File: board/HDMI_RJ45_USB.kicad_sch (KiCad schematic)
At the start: 10 parts, among them J1 RJ45, J2 Micro_SD_Card_Det, U1 HDMI/USB, U11 TPD4EUSB30, U12 RT9742GGJ5, U5 RT9742GGJ5, U6 TPD4EUSB30

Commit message: updated most stuff, but i completely redid the diff pairs
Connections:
- net TRD1_N: now also U6.1 (D1+); no longer U6.2 (D1-)
- net TRD1_P: now also U6.2 (D1-); no longer U6.1 (D1+)
- net TRD2_N: now also U11.5 (D2-); no longer U11.4 (D2+)
- net TRD2_P: now also U11.4 (D2+); no longer U11.5 (D2-)
- net TRD3_N: now also U11.1 (D1+); no longer U11.2 (D1-)
- net TRD3_P: now also U11.2 (D1-); no longer U11.1 (D1+)

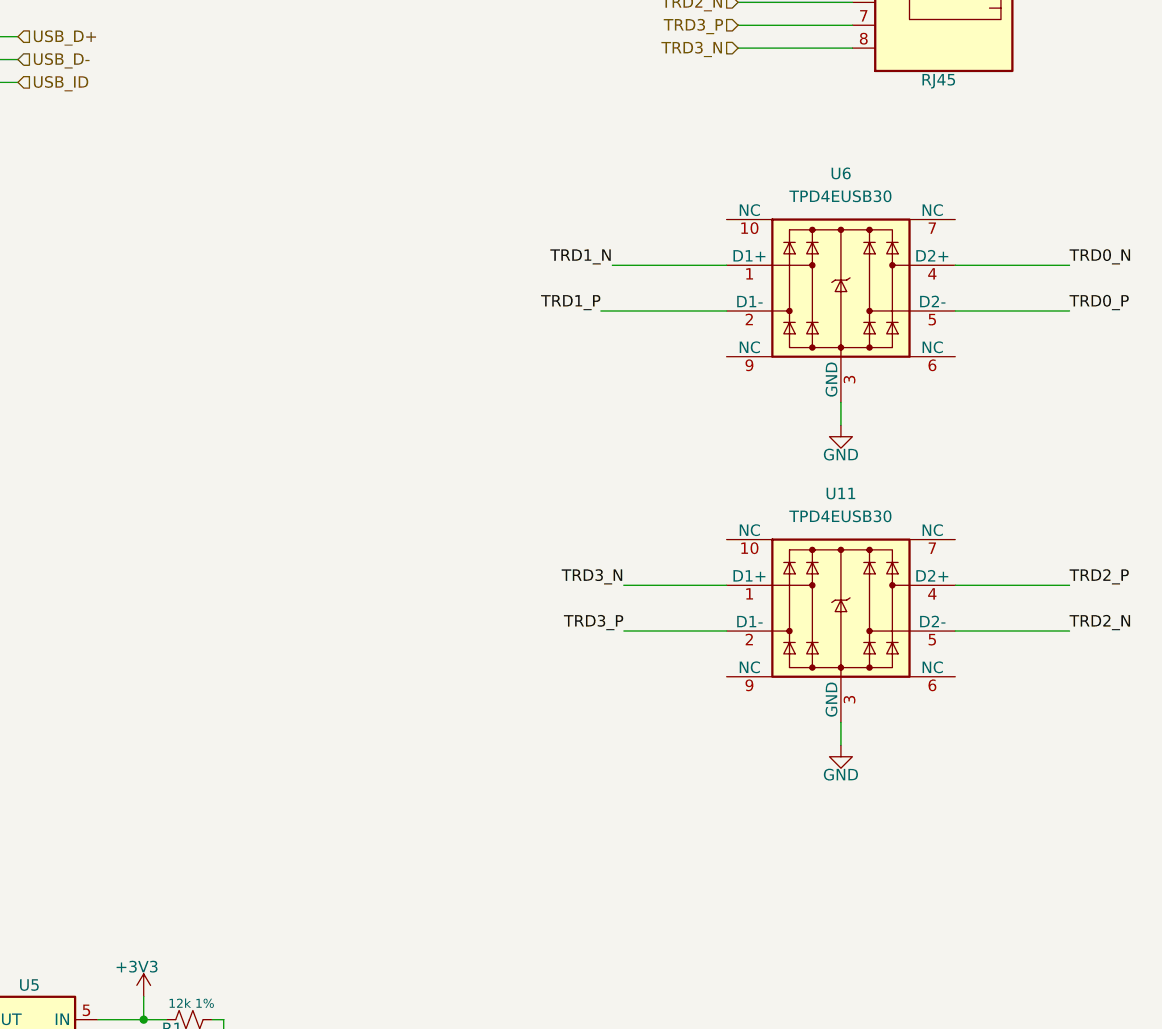
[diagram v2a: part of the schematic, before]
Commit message: going to add the magnetic transformer which will messs a lot of stuff up
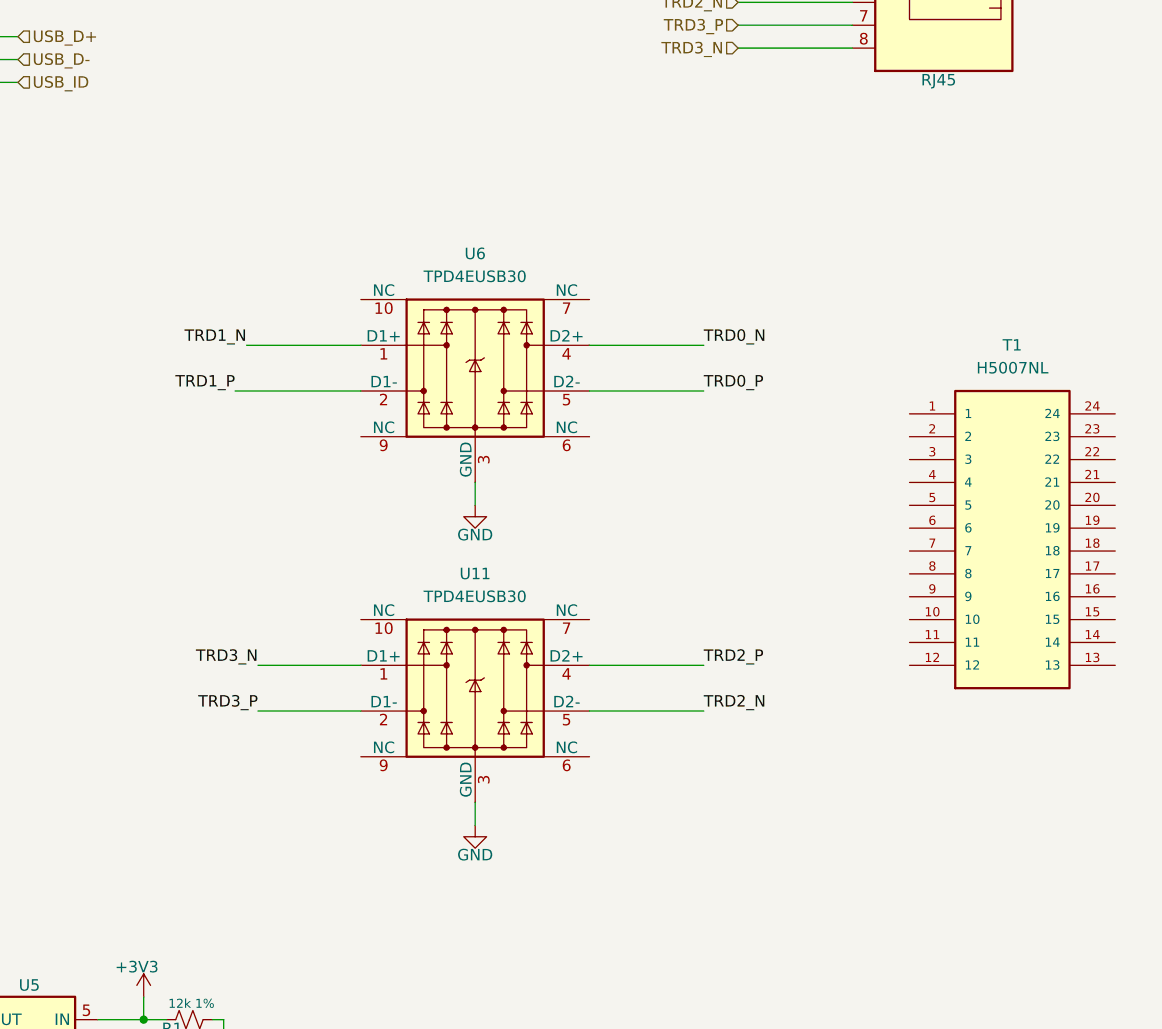
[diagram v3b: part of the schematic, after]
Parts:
- added T1: H5007NL, H5007NL:SOIC127P1600X551-24N, symbol H5007NL:H5007NL
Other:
- moved on the sheet: U11, U6

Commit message: started more ethernet adding stuff
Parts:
- added C13, C15, C16, C2: C_Small, Capacitor_SMD:C_0402_1005Metric, symbol Device:C_Small
- added R14, R15, R16, R17: 75, Resistor_SMD:R_0402_1005Metric, symbol Device:R_Small_US
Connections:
- net GND: now also C13.1, C15.1, C16.1, C2.1, R14.1, R15.1, R16.1, R17.1
- net TRD0_N: now also T1.2 (TD1+); no longer J1.2, U6.4 (D2+)
- net TRD0_P: now also T1.3 (TD1-); no longer J1.1, U6.5 (D2-)
- net TRD1_N: now also T1.5 (TD2+), U11.2 (D1-); no longer J1.4, U6.1 (D1+)
- net TRD1_P: now also T1.6 (TD2-), U11.1 (D1+); no longer J1.3, U6.2 (D1-)
- net TRD2_N: now also T1.8 (TD3+), U6.4 (D2+); no longer J1.6, U11.5 (D2-)
- net TRD2_P: now also T1.9 (TD3-), U6.5 (D2-); no longer J1.5, U11.4 (D2+)
- net TRD3_N: now also T1.11 (TD4+), U6.1 (D1+); no longer J1.8, U11.1 (D1+)
- net TRD3_P: now also T1.12 (TD4-), U6.2 (D1-); no longer J1.7, U11.2 (D1-)
- net at T1.1 (TCT1): now also C16.2
- net at T1.10 (TCT4): now also C15.2
- net MX3_P: now reaches T1.13 (MX4-)
- net MX3_N: now reaches T1.14 (MX4+)
- net MCT3: now reaches T1.15 (MCT4)
- net MCT3: now also R17.2
- net MX2_P: now reaches T1.16 (MX3-)
- net MX2_N: now reaches T1.17 (MX3+)
- net MCT2: now reaches T1.18 (MCT3)
- net MCT2: now also R16.2
- net MX1_P: now reaches T1.19 (MX2-)
- net MX1_N: now reaches T1.20 (MX2+)
- net MCT1: now reaches T1.21 (MCT2)
- net MCT1: now also R15.2
- net MX0_P: now reaches T1.22 (MX1-)
- net MX0_N: now reaches T1.23 (MX1+)
- net MCT0: now reaches T1.24 (MCT1)
- net MCT0: now also R14.2
- net at T1.4 (TCT2): now also C2.2
- net at T1.7 (TCT3): now also C13.2
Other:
- moved on the sheet: J1, T1

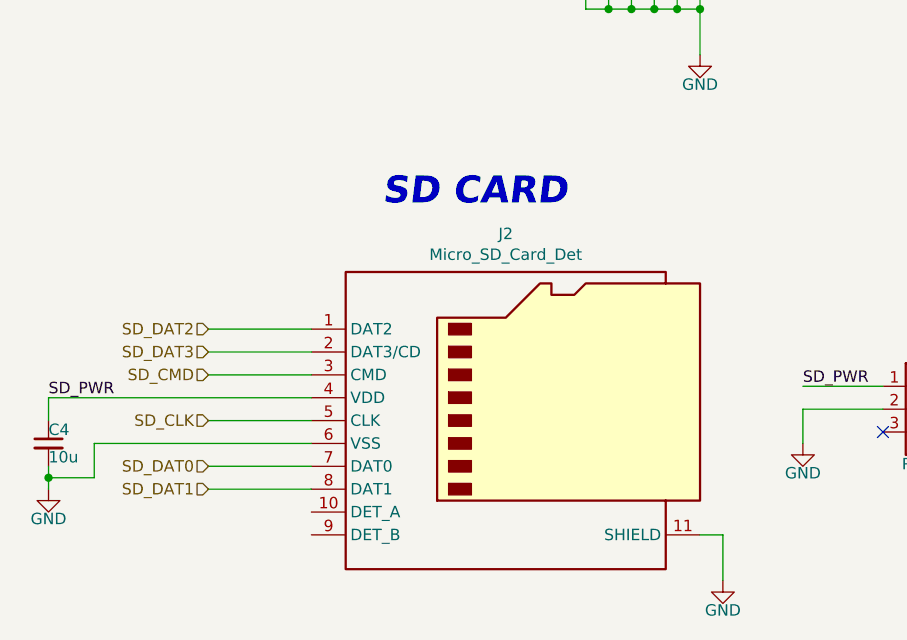
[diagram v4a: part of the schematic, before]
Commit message: added the real micro sd card slot
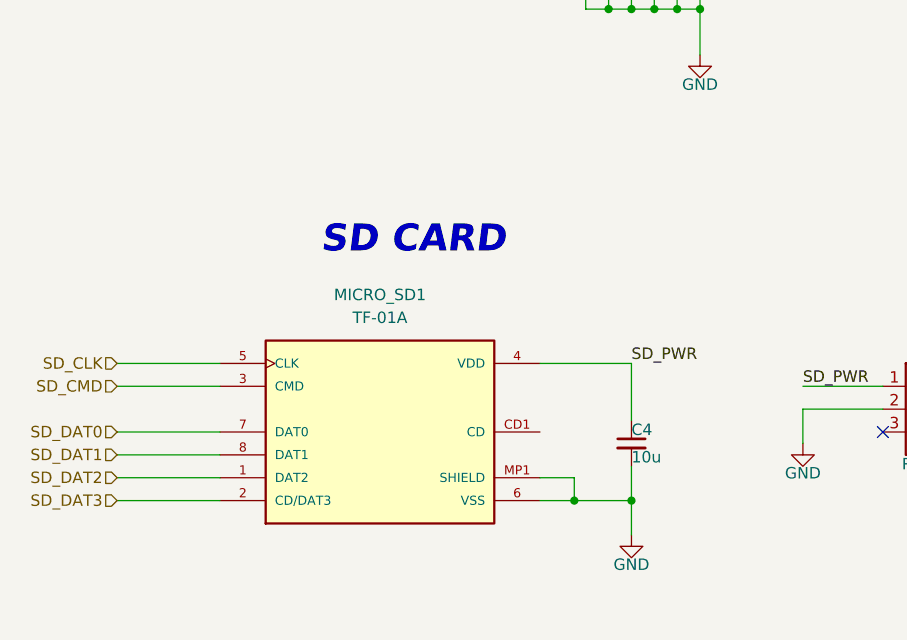
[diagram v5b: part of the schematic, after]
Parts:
- removed J2: Micro_SD_Card_Det, greencharge-footprints:MICRO_SD_MOLEX_503398-1892, symbol Connector:Micro_SD_Card_Det
- added MICRO_SD1: TF-01A, MicroSD:TF-01A, symbol MicroSd:TF-01A
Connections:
- net GND: now also MICRO_SD1.6 (VSS), MICRO_SD1.MP1 (SHIELD), MICRO_SD1.MP2 (SHIELD), MICRO_SD1.MP3 (SHIELD), MICRO_SD1.MP4 (SHIELD)
- net SD_CLK: now also MICRO_SD1.5 (CLK)
- net SD_CMD: now also MICRO_SD1.3 (CMD)
- net SD_DAT0: now also MICRO_SD1.7 (DAT0)
- net SD_DAT1: now also MICRO_SD1.8 (DAT1)
- net SD_DAT2: now also MICRO_SD1.1 (DAT2)
- net SD_DAT3: now also MICRO_SD1.2 (CD/DAT3)
- net SD_PWR: now also MICRO_SD1.4 (VDD)
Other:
- moved on the sheet: C4
